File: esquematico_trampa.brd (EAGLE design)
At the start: 88.9 x 93.7 mm, 17 parts, among them U1 MICROCHIP_MCP3008-I-PMICROCHI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, U2 LM358PE3

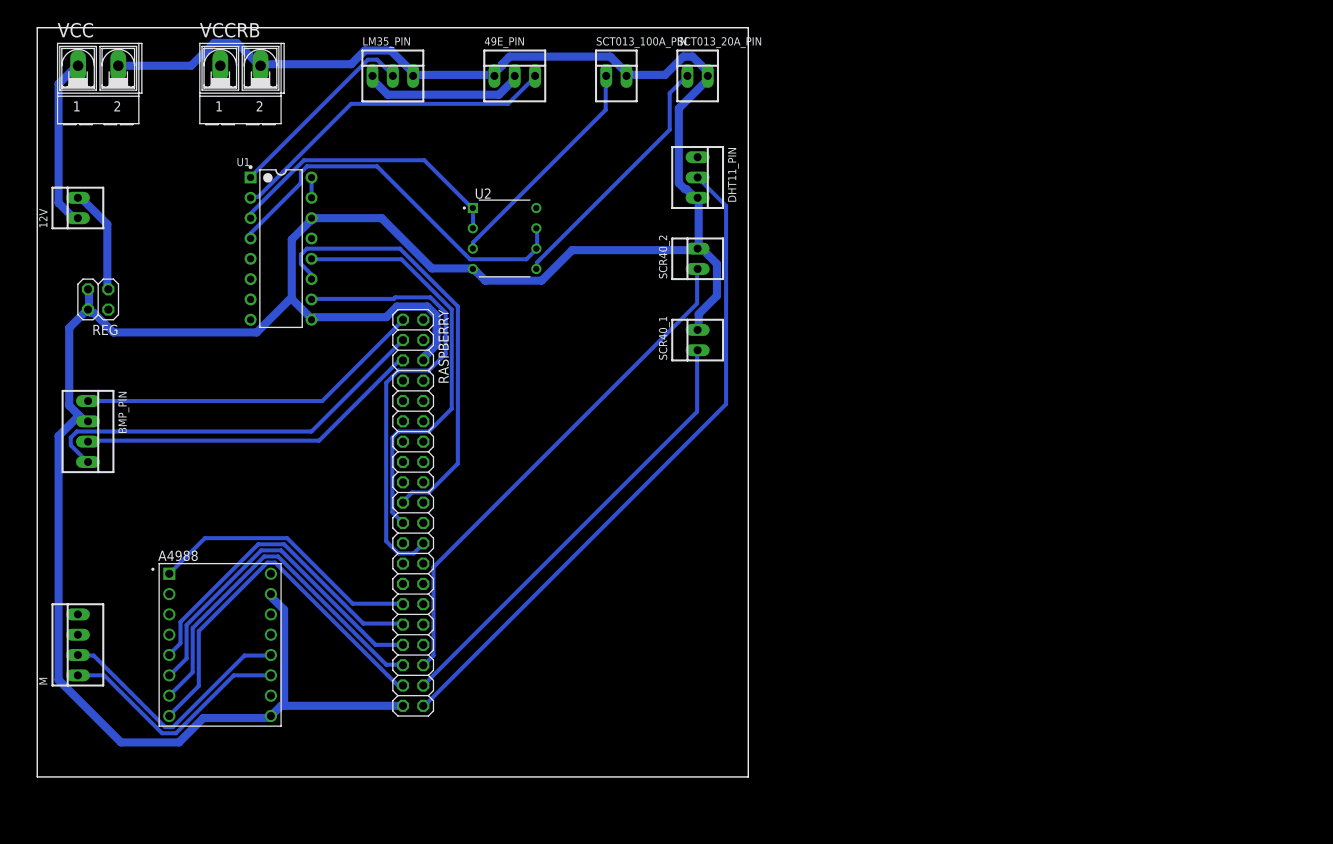
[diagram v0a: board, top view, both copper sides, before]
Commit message: diseño 90% de routeo
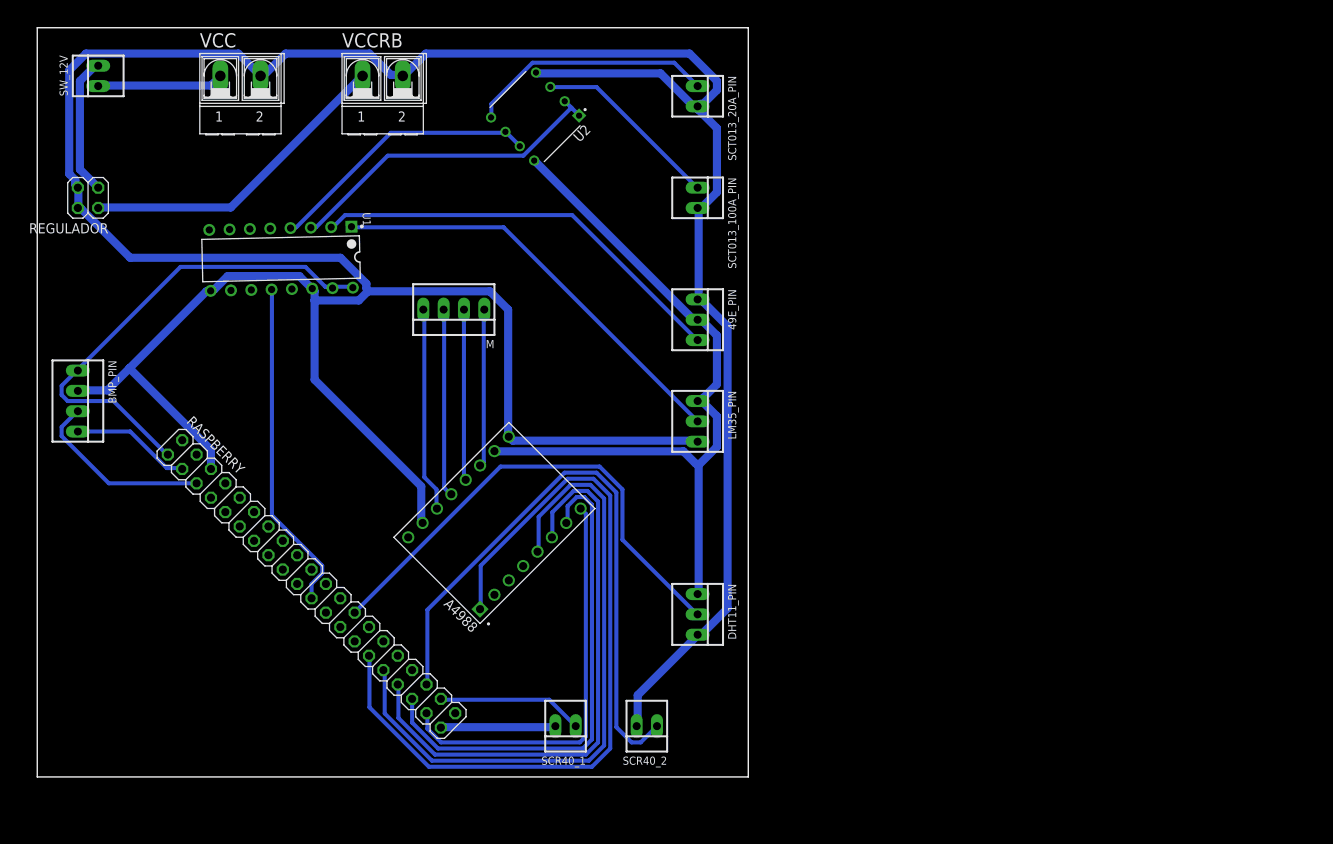
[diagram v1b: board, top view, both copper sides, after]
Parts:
- removed 12V: 22-23-2021, con-molex:22-23-2021
- removed REG: (no value), pinhead:2X02
- added REGULADOR: (no value), pinhead:2X02
- added SW_12V: 22-23-2021, con-molex:22-23-2021
- moved M 63.0 mm to (52.1, 64.8), turned to 180 degrees
- moved SCR40_2 58.8 mm to (76.2, 12.7), turned to 180 degrees
- moved LM35_PIN 57.6 mm to (82.5, 50.8), turned to 270 degrees
- moved DHT11_PIN 54.6 mm to (82.5, 26.7)
- moved SCR40_1 51.0 mm to (66.0, 12.7), turned to 180 degrees
- moved 49E_PIN 38.1 mm to (82.5, 63.5), turned to 270 degrees
- moved A4988 37.5 mm to (57.1, 38.1), turned to 135 degrees
- moved SCT013_100A_PIN 18.3 mm to (82.5, 78.7), turned to 270 degrees
- moved VCCRB 17.8 mm to (43.2, 94.0)
- moved VCC 17.8 mm to (25.4, 94.0)
- moved U2 15.7 mm to (62.2, 88.9), turned to 225 degrees
- moved RASPBERRY 15.5 mm to (34.3, 30.5), turned to 315 degrees
- moved BMP_PIN 4.02 mm to (5.08, 53.3)
- moved SCT013_20A_PIN 2.54 mm to (82.5, 91.4), turned to 270 degrees
- moved U1 1.27 mm to (30.5, 71.1), turned to 271.3 degrees
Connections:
- removed net 12+: 12V.1, VCC.1
- removed net GPIO21: DHT11_PIN.2, RASPBERRY.40
- removed net IN5+: REG.2, VCCRB.1
- new net GPIO7: DHT11_PIN.2, RASPBERRY.26
- new net IN12+: REGULADOR.1, SW_12V.2
- new net OUT12+: SW_12V.1, VCC.1
- new net OUT5+: REGULADOR.2, VCCRB.1
- net GND: now also REGULADOR.3, REGULADOR.4; no longer REG.3, REG.4
- net SW12: no longer 12V.2, REG.1
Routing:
- net GPIO21: track 83.3 -> 0.00 mm
- net 5V: track 20.2 -> 93.9 mm
- net GND: track 355.2 -> 427.1 mm
- net GPIO5: track 34.5 -> 99.2 mm
- net GPIO7: track 0.00 -> 61.8 mm
- net SPICE0: track 57.4 -> 0.00 mm
- net SPMOS1: track 55.1 -> 0.00 mm
- net GPIO6: track 40.8 -> 82.0 mm
- net OUT5+: track 0.00 -> 39.9 mm
- net GPIO20: track 56.1 -> 18.3 mm
- net SDA_I2C: track 50.6 -> 15.0 mm
- net GPIO13: track 43.0 -> 72.4 mm
- net V_LM35: track 24.8 -> 53.3 mm
- net 2B: track 0.00 -> 25.6 mm
- net 2A: track 0.00 -> 23.6 mm
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
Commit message: esquematico ordenado y board 100 ruteado
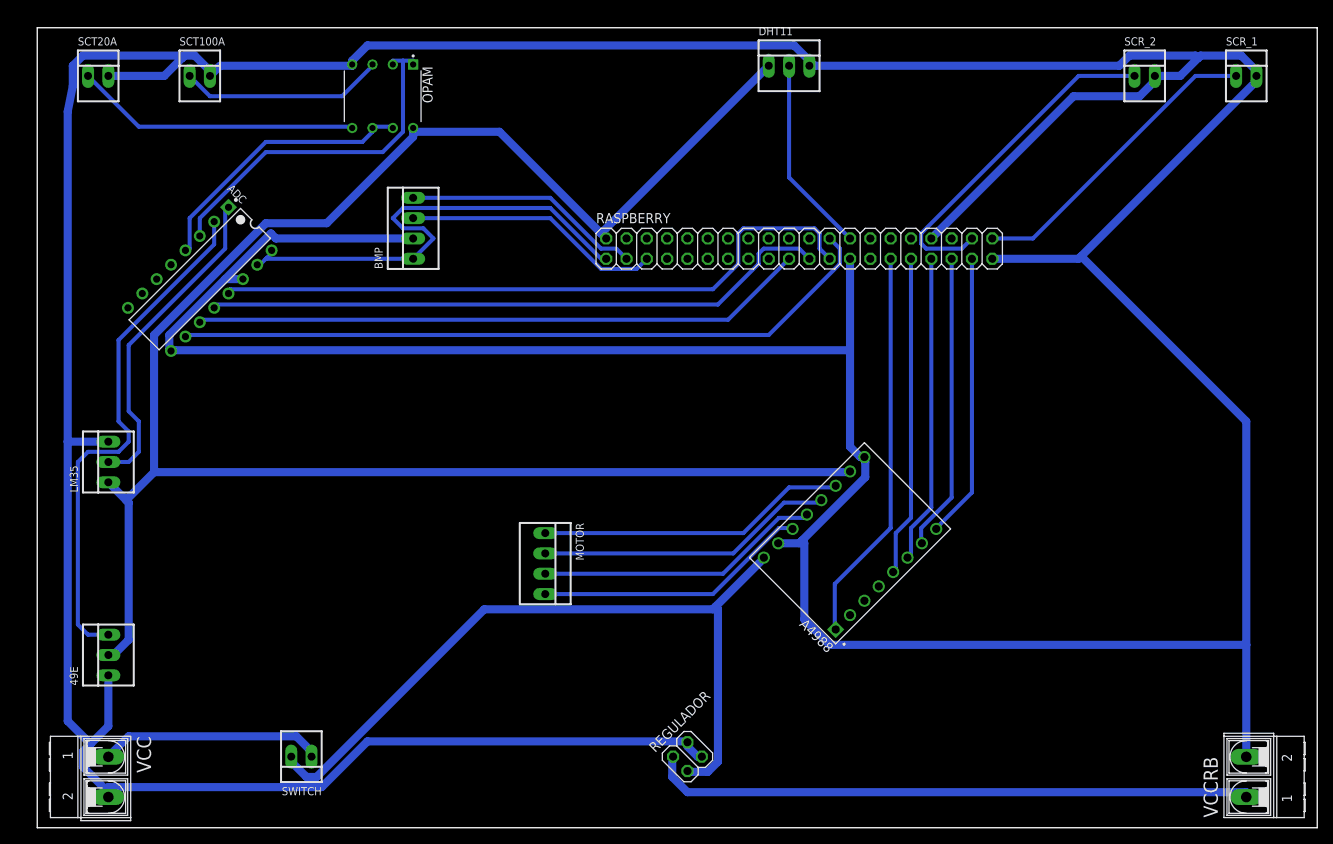
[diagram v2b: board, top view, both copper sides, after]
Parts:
- removed 49E_PIN, DHT11_PIN, LM35_PIN: 22-23-2031, con-molex:22-23-2031
- removed BMP_PIN, M: 22-23-2041, con-molex:22-23-2041
- removed SCR40_1, SCR40_2, SCT013_100A_PIN, SCT013_20A_PIN: 22-23-2021, con-molex:22-23-2021
- removed U1: MICROCHIP_MCP3008-I-PMICROCHIP_MCP3008-I-P_0_0, P:MICROCHIP_MCP3008-I-P_0
- removed U2: LM358PE3, LM358PE3:DIP794W45P254L959H508Q8
- added 49E, DHT11, LM35: 22-23-2031, con-molex:22-23-2031
- added ADC: MICROCHIP_MCP3008-I-PMICROCHIP_MCP3008-I-P_0_0, P:MICROCHIP_MCP3008-I-P_0
- added BMP, MOTOR: 22-23-2041, con-molex:22-23-2041
- added OPAM: LM358PE3, LM358PE3:DIP794W45P254L959H508Q8
- added SCR_1, SCR_2, SCT100A, SWITCH: 22-23-2021, con-molex:22-23-2021
- moved VCCRB 139.0 mm to (151.1, 6.35), turned to 90 degrees
- moved REGULADOR 102.4 mm to (81.3, 8.89), turned to 45 degrees
- moved VCC 89.2 mm to (8.89, 6.35), turned to 270 degrees
- moved RASPBERRY 74.0 mm to (95.2, 72.4), turned to 0 degrees
- moved A4988 44.5 mm to (101.6, 35.6)
- turned SCT20A to 0 degrees
- renumbered SW_12V to SCT20A
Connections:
- removed net GPIO16: RASPBERRY.36, SCR40_2.1
- removed net SW12: A4988.16
- new net GPIO21: RASPBERRY.40, SCR_1.1
- net 1A: now also MOTOR.2; no longer M.2
- net 1B: now also MOTOR.1; no longer M.1
- net 2A: now also MOTOR.3; no longer M.3
- net 2B: now also MOTOR.4; no longer M.4
- net 3.3V: now also ADC.15, ADC.16, BMP.1; no longer BMP_PIN.1, U1.15, U1.16
- net 5V: now also 49E.2, DHT11.1, LM35.1, OPAM.8; no longer 49E_PIN.2, DHT11_PIN.1, LM35_PIN.1, U2.8
- net GND: now also 49E.1, ADC.14, ADC.9, BMP.2, DHT11.3, LM35.3, OPAM.4, RASPBERRY.25, RASPBERRY.34, SCR_1.2, SCR_2.2, SCT100A.2, SCT20A.2; no longer 49E_PIN.1, BMP_PIN.2, DHT11_PIN.3, LM35_PIN.3, RASPBERRY.6, SCR40_1.2, SCR40_2.2, SCT013_100A_PIN.2, SCT013_20A_PIN.2, U1.14, U1.9, U2.4
- net GPIO20: now also SCR_2.1; no longer SCR40_1.1
- net GPIO7: now also DHT11.2; no longer DHT11_PIN.2
- net IN12+: now also A4988.16, SWITCH.2; no longer SCT20A.2
- net OUT12+: now also SWITCH.1; no longer SCT20A.1
- net OUT_SCT100: now also OPAM.3, SCT100A.1; no longer SCT013_100A_PIN.1, U2.3
- net OUT_SCT20: now also OPAM.5, SCT20A.1; no longer SCT013_20A_PIN.1, U2.5
- net SCL_I2C: now also BMP.3; no longer BMP_PIN.3
- net SDA_I2C: now also BMP.4; no longer BMP_PIN.4
- net SPICE0: now also ADC.10; no longer U1.10
- net SPMIS0: now also ADC.12; no longer U1.12
- net SPMOS1: now also ADC.11; no longer U1.11
- net SPSCLK: now also ADC.13; no longer U1.13
- net V_49E: now also 49E.3, ADC.2; no longer 49E_PIN.3, U1.2
- net V_LM35: now also ADC.1, LM35.2; no longer LM35_PIN.2, U1.1
- net V_SCT100: now also ADC.3, OPAM.1, OPAM.2; no longer U1.3, U2.1, U2.2
- net V_SCT20: now also ADC.4, OPAM.6, OPAM.7; no longer U1.4, U2.6, U2.7
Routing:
- net GND: track 427.1 -> 745.6 mm
- net 5V: track 93.9 -> 236.3 mm
- net SPICE0: track 0.00 -> 89.2 mm
- net SPSCLK: track 0.00 -> 83.6 mm
- net IN12+: track 17.4 -> 95.8 mm
- net GPIO16: track 77.2 -> 0.00 mm
- net SPMOS1: track 0.00 -> 77.1 mm
- net GPIO5: track 99.2 -> 49.2 mm
- net GPIO6: track 82.0 -> 40.1 mm
- net GPIO21: track 0.00 -> 38.9 mm
- net SPMIS0: track 41.8 -> 78.9 mm
- net GPIO7: track 61.8 -> 24.7 mm
- net OUT5+: track 39.9 -> 75.8 mm
- net GPIO13: track 72.4 -> 38.6 mm
- net GPIO19: track 62.8 -> 37.2 mm
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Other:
- board size 88.9 x 93.7 mm -> 160 x 100 mm
